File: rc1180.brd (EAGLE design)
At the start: 30 x 49.5 mm, 16 parts, among them J1 47642-0001, U1 CH340C, U2 AMS1117, X1 SMA-142-0701-801/806

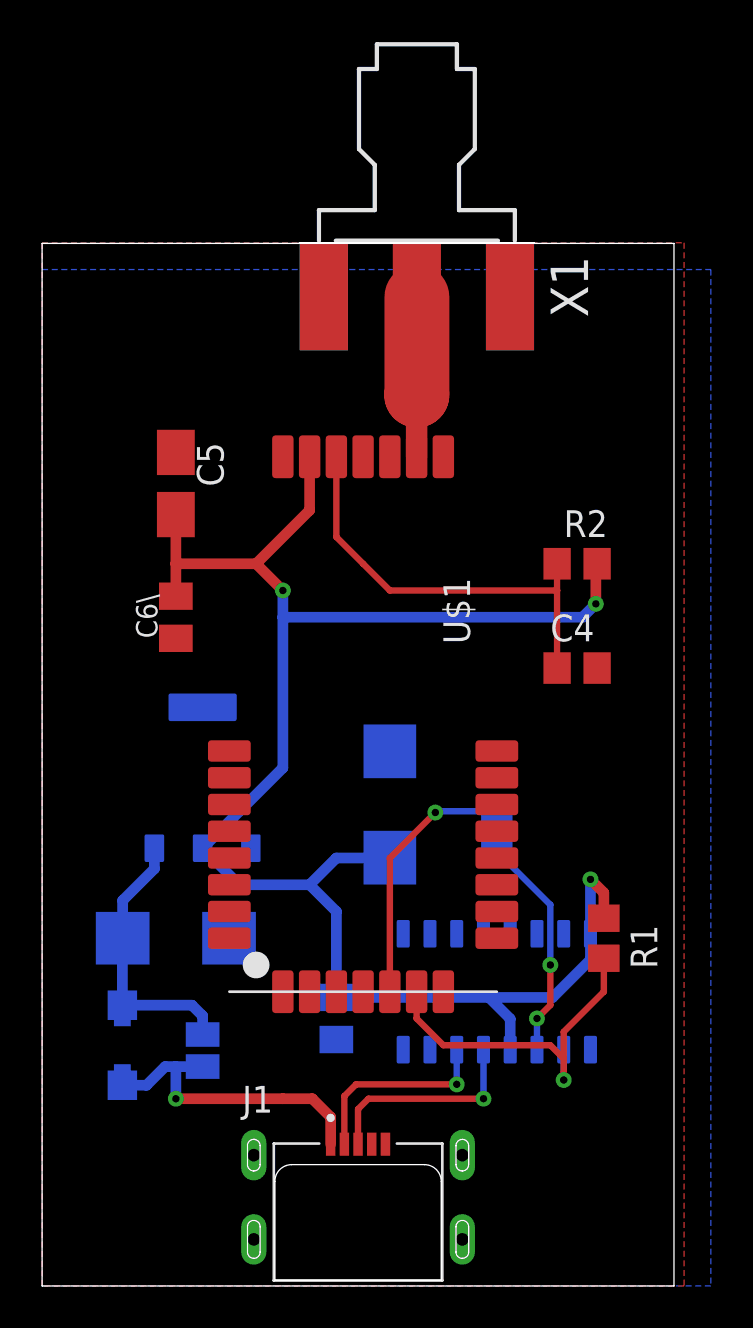
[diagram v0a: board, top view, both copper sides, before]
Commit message: Added holes and vias
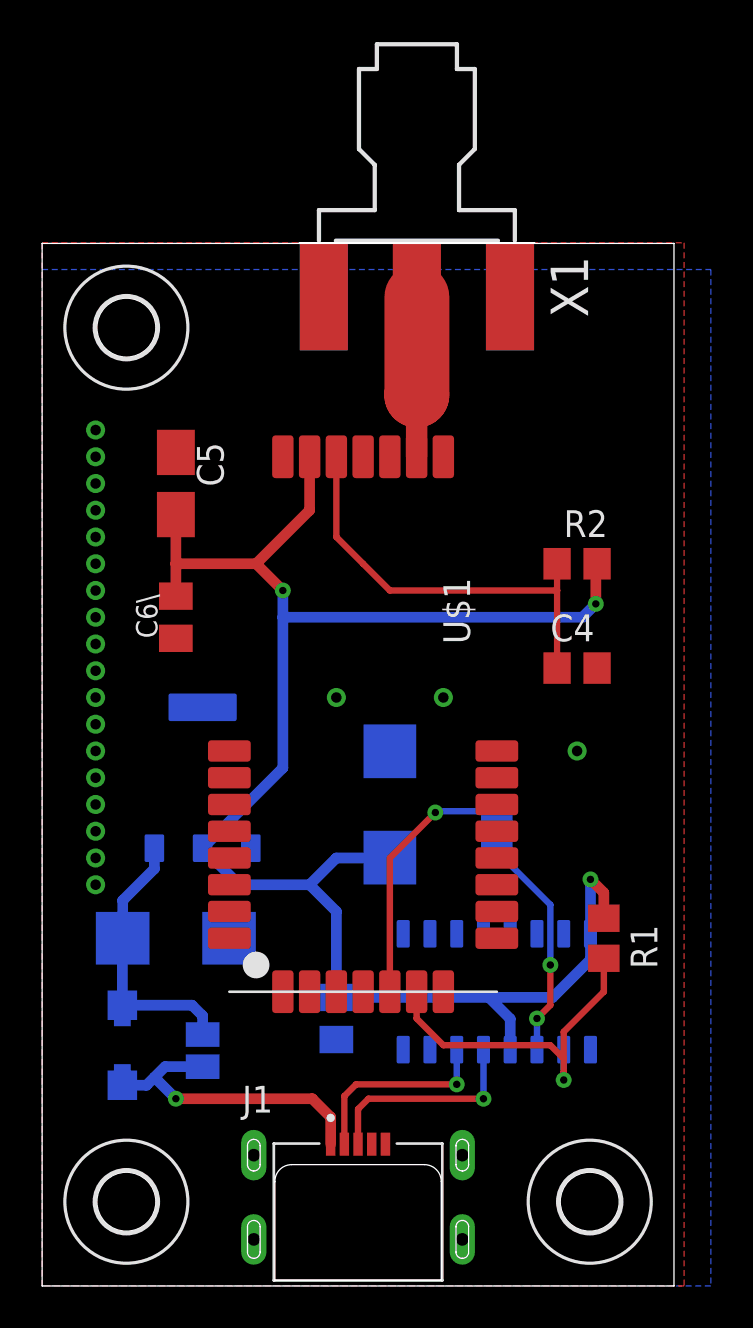
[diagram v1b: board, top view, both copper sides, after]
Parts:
- added H1, H2, H3: MOUNT-HOLE2.8, holes:2,8
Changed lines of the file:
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@@
 <layer number="19" name="Unrouted" color="6" fill="1" visible="yes" active="yes"/>
 <layer number="20" name="Dimension" color="24" fill="1" visible="yes" active="yes"/>
-<layer number="21" name="tPlace" color="7" fill="1" visible="no" active="yes"/>
-<layer number="22" name="bPlace" color="7" fill="1" visible="yes" active="yes"/>
-<layer number="23" name="tOrigins" color="15" fill="1" visible="no" active="yes"/>
-<layer number="24" name="bOrigins" color="15" fill="1" visible="yes" active="yes"/>
-<layer number="25" name="tNames" color="7" fill="1" visible="no" active="yes"/>
-<layer number="26" name="bNames" color="7" fill="1" visible="yes" active="yes"/>
+<layer number="21" name="tPlace" color="7" fill="1" visible="yes" active="yes"/>
+<layer number="22" name="bPlace" color="7" fill="1" visible="no" active="yes"/>
+<layer number="23" name="tOrigins" color="15" fill="1" visible="yes" active="yes"/>
+<layer number="24" name="bOrigins" color="15" fill="1" visible="no" active="yes"/>
+<layer number="25" name="tNames" color="7" fill="1" visible="yes" active="yes"/>
+<layer number="26" name="bNames" color="7" fill="1" visible="no" active="yes"/>
 <layer number="27" name="tValues" color="7" fill="1" visible="no" active="yes"/>
 <layer number="28" name="bValues" color="7" fill="1" visible="no" active="yes"/>
@@
 <layer number="37" name="tTest" color="7" fill="1" visible="no" active="yes"/>
 <layer number="38" name="bTest" color="7" fill="1" visible="no" active="yes"/>
-<layer number="39" name="tKeepout" color="4" fill="11" visible="no" active="yes"/>
-<layer number="40" name="bKeepout" color="1" fill="11" visible="yes" active="yes"/>
-<layer number="41" name="tRestrict" color="4" fill="10" visible="no" active="yes"/>
-<layer number="42" name="bRestrict" color="1" fill="10" visible="yes" active="yes"/>
+<layer number="39" name="tKeepout" color="4" fill="11" visible="yes" active="yes"/>
+<layer number="40" name="bKeepout" color="1" fill="11" visible="no" active="yes"/>
+<layer number="41" name="tRestrict" color="4" fill="10" visible="yes" active="yes"/>
+<layer number="42" name="bRestrict" color="1" fill="10" visible="no" active="yes"/>
 <layer number="43" name="vRestrict" color="2" fill="10" visible="no" active="yes"/>
 <layer number="44" name="Drills" color="7" fill="1" visible="no" active="yes"/>
-<layer number="45" name="Holes" color="7" fill="1" visible="no" active="yes"/>
+<layer number="45" name="Holes" color="7" fill="1" visible="yes" active="yes"/>
 <layer number="46" name="Milling" color="3" fill="1" visible="no" active="yes"/>
 <layer number="47" name="Measures" color="7" fill="1" visible="no" active="yes"/>
 <layer number="48" name="Document" color="7" fill="1" visible="no" active="yes"/>
 <layer number="49" name="Reference" color="7" fill="1" visible="no" active="yes"/>
-<layer number="51" name="tDocu" color="7" fill="1" visible="no" active="yes"/>
-<layer number="52" name="bDocu" color="7" fill="1" visible="yes" active="yes"/>
+<layer number="51" name="tDocu" color="7" fill="1" visible="yes" active="yes"/>
+<layer number="52" name="bDocu" color="7" fill="1" visible="no" active="yes"/>
 <layer number="88" name="SimResults" color="9" fill="1" visible="no" active="no"/>
 <layer number="89" name="SimProbes" color="9" fill="1" visible="no" active="no"/>
@@
 <attribute name="VALUE" x="8.904" y="48.26" size="1.778" layer="27" rot="R270"/>
 </element>
+<element name="H1" library="holes" library_urn="urn:adsk.eagle:library:237" package="2,8" package3d_urn="urn:adsk.eagle:package:14271/1" value="MOUNT-HOLE2.8" x="26" y="4" smashed="yes">
+<attribute name="POPULARITY" value="15" x="26" y="4" size="1.778" layer="27" display="off"/>
+</element>
+<element name="H2" library="holes" library_urn="urn:adsk.eagle:library:237" package="2,8" package3d_urn="urn:adsk.eagle:package:14271/1" value="MOUNT-HOLE2.8" x="4" y="4" smashed="yes">
+<attribute name="POPULARITY" value="15" x="4" y="4" size="1.778" layer="27" display="off"/>
+</element>
+<element name="H3" library="holes" library_urn="urn:adsk.eagle:library:237" package="2,8" package3d_urn="urn:adsk.eagle:package:14271/1" value="MOUNT-HOLE2.8" x="4" y="45.5" smashed="yes">
+<attribute name="POPULARITY" value="15" x="4" y="45.5" size="1.778" layer="27" display="off"/>
+</element>
 </elements>
 <signals>
@@
 <vertex x="30.48" y="0"/>
 </polygon>
+<via x="13.97" y="27.94" extent="1-16" drill="0.5"/>
+<via x="19.05" y="27.94" extent="1-16" drill="0.5"/>
+<via x="25.4" y="25.4" extent="1-16" drill="0.5"/>
+<via x="2.54" y="24.13" extent="1-16" drill="0.5"/>
+<via x="2.54" y="25.4" extent="1-16" drill="0.5"/>
+<via x="2.54" y="26.67" extent="1-16" drill="0.5"/>
+<via x="2.54" y="27.94" extent="1-16" drill="0.5"/>
+<via x="2.54" y="29.21" extent="1-16" drill="0.5"/>
+<via x="2.54" y="30.48" extent="1-16" drill="0.5"/>
+<via x="2.54" y="31.75" extent="1-16" drill="0.5"/>
+<via x="2.54" y="33.02" extent="1-16" drill="0.5"/>
+<via x="2.54" y="34.29" extent="1-16" drill="0.5"/>
+<via x="2.54" y="35.56" extent="1-16" drill="0.5"/>
+<via x="2.54" y="36.83" extent="1-16" drill="0.5"/>
+<via x="2.54" y="38.1" extent="1-16" drill="0.5"/>
+<via x="2.54" y="39.37" extent="1-16" drill="0.5"/>
+<via x="2.54" y="40.64" extent="1-16" drill="0.5"/>
+<via x="2.54" y="22.86" extent="1-16" drill="0.5"/>
+<via x="2.54" y="21.59" extent="1-16" drill="0.5"/>
+<via x="2.54" y="20.32" extent="1-16" drill="0.5"/>
+<via x="2.54" y="19.05" extent="1-16" drill="0.5"/>
 </signal>
 <signal name="+3V3">
@@
 <contactref element="U$2" pad="A"/>
 <contactref element="SJ1" pad="1"/>
-<wire x1="11.43" y1="8.89" x2="6.35" y2="8.89" width="0.508" layer="1"/>
+<wire x1="12.827" y1="8.89" x2="6.35" y2="8.89" width="0.508" layer="1"/>
 <via x="6.35" y="8.89" extent="1-16" drill="0.35"/>
-<wire x1="7.62" y1="10.414" x2="7.366" y2="10.16" width="0.508" layer="16"/>
-<wire x1="4.958" y1="9.53" x2="3.81" y2="9.53" width="0.508" layer="16"/>
-<wire x1="7.62" y1="10.414" x2="6.35" y2="10.414" width="0.508" layer="16"/>
-<wire x1="6.35" y1="10.414" x2="5.842" y2="10.414" width="0.508" layer="16"/>
-<wire x1="5.842" y1="10.414" x2="4.958" y2="9.53" width="0.508" layer="16"/>
-<wire x1="6.35" y1="8.89" x2="6.35" y2="10.414" width="0.508" layer="16"/>
+<wire x1="3.81" y1="9.53" x2="4.958" y2="9.53" width="0.508" layer="16"/>
+<wire x1="7.62" y1="10.414" x2="5.842" y2="10.414" width="0.508" layer="16"/>
+<wire x1="5.842" y1="10.414" x2="5.334" y2="9.906" width="0.508" layer="16"/>
+<wire x1="5.334" y1="9.906" x2="4.958" y2="9.53" width="0.508" layer="16"/>
 <wire x1="13.7" y1="6.731" x2="13.7" y2="8.017" width="0.508" layer="1"/>
-<wire x1="12.827" y1="8.89" x2="11.43" y2="8.89" width="0.508" layer="1"/>
 <wire x1="13.7" y1="8.017" x2="12.827" y2="8.89" width="0.508" layer="1"/>
+<wire x1="6.35" y1="8.89" x2="5.334" y2="9.906" width="0.508" layer="16"/>
 </signal>
 </signals>
